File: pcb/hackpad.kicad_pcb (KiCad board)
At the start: 2 copper layers, 90 x 70 mm, 16 parts, among them J1 XIAO_L, J2 XIAO_R, J3 OLED, SW1 MX, SW2 MX, SW3 MX, SW4 MX

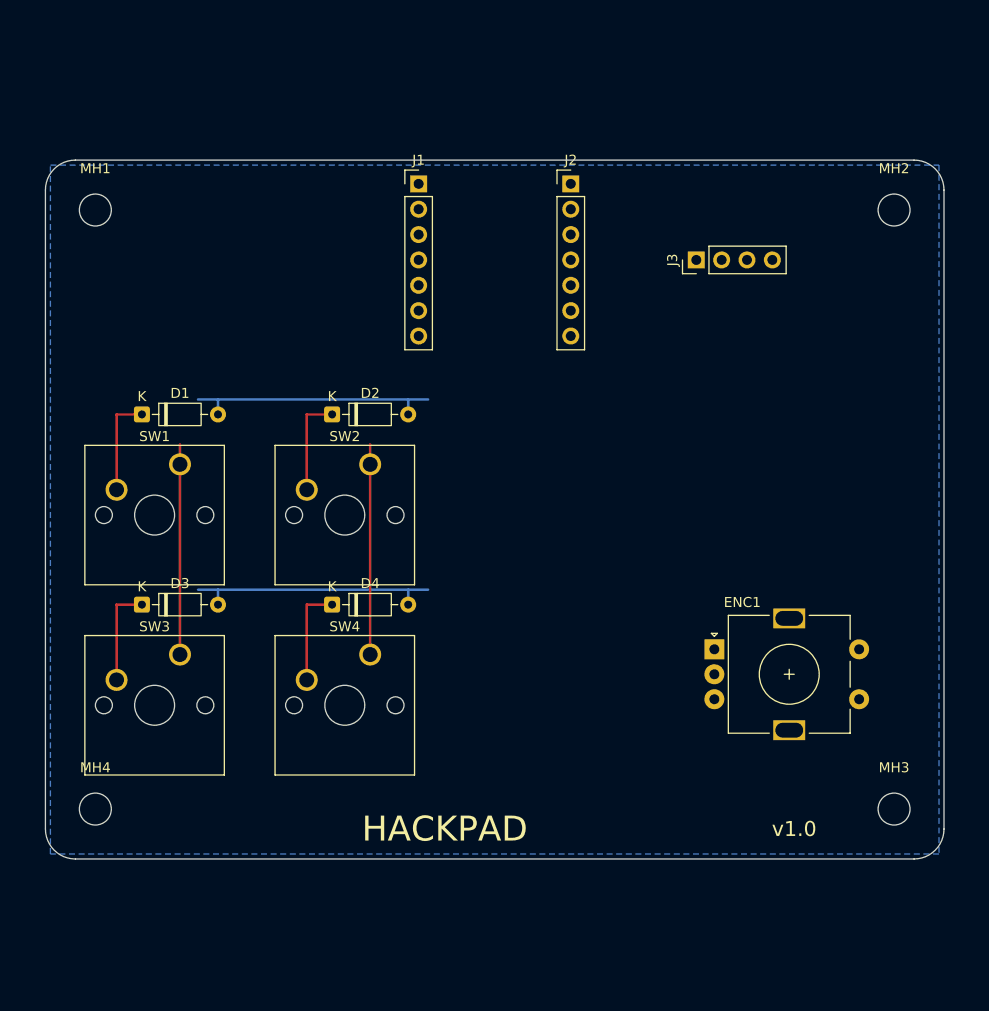
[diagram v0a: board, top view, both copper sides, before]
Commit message: v2: max-loaded build — 12 keys (4x3 matrix) + EC11 encoder + OLED
Surveyed 389 hackpads in hackclub/hackpad. Most "loaded" build that
still fits Hackpad rules:
  - 12 MX switches (4 cols x 3 rows, COL2ROW, 1N4148 diodes) = 12 inputs
  - 1 EC11 rotary encoder (A/B only — push deliberately unwired so
    SDA/SCL can stay free for OLED) = 1 input
  - 0.91" SSD1306 128x32 OLED on I2C1
  - 13 total inputs (under 16-input cap)
  - 95 x 95 mm board (under 100x100 cap)
  - All 11 usable XIAO RP2040 GPIO consumed (none spare)

PCB:
  - Matrix fully routed in copper (4 COL trunks F.Cu, 3 ROW trunks B.Cu
    with cathode tabs, 12 switch->anode bridges, GND pour, edge cuts)
  - 11 short XIAO->peripheral pulls left as ratlines for ~5 min
    interactive routing (each with exact start/end coords in
    pcb/HOW_TO_FINISH.md)
  - DRC passes at error level (0 violations, 0 unconnected)
  - New silkscreen: HACKPAD v2.0 front, github URL on back

Hardware as individual STL/STEP parts:
  - production/Top.{stl,step}                 (3D-printable)
  - production/Bottom.{stl,step}              (3D-printable)
  - production/M3x16_Screw.{stl,step}         (used x4 in assembly)
  - production/HeatsetInsert_M3x5x4.{stl,step} (used x4 in assembly)
  - cad/assembled-model.{step,stl} now includes the 4 screws + 4 inserts

Firmware: KMK with 3 layers (default letters / media / numpad), encoder
re-mapped per layer. OLED shows active layer name.

Mockup re-rendered to show the 12-key grid with 4 visible screw heads,
encoder knob, OLED window, HACK CLUB decal — saved to assets/mockup.png
and ~/Desktop/hackpad_mockup.png.

Re-exported production/gerbers.zip from the new .kicad_pcb.
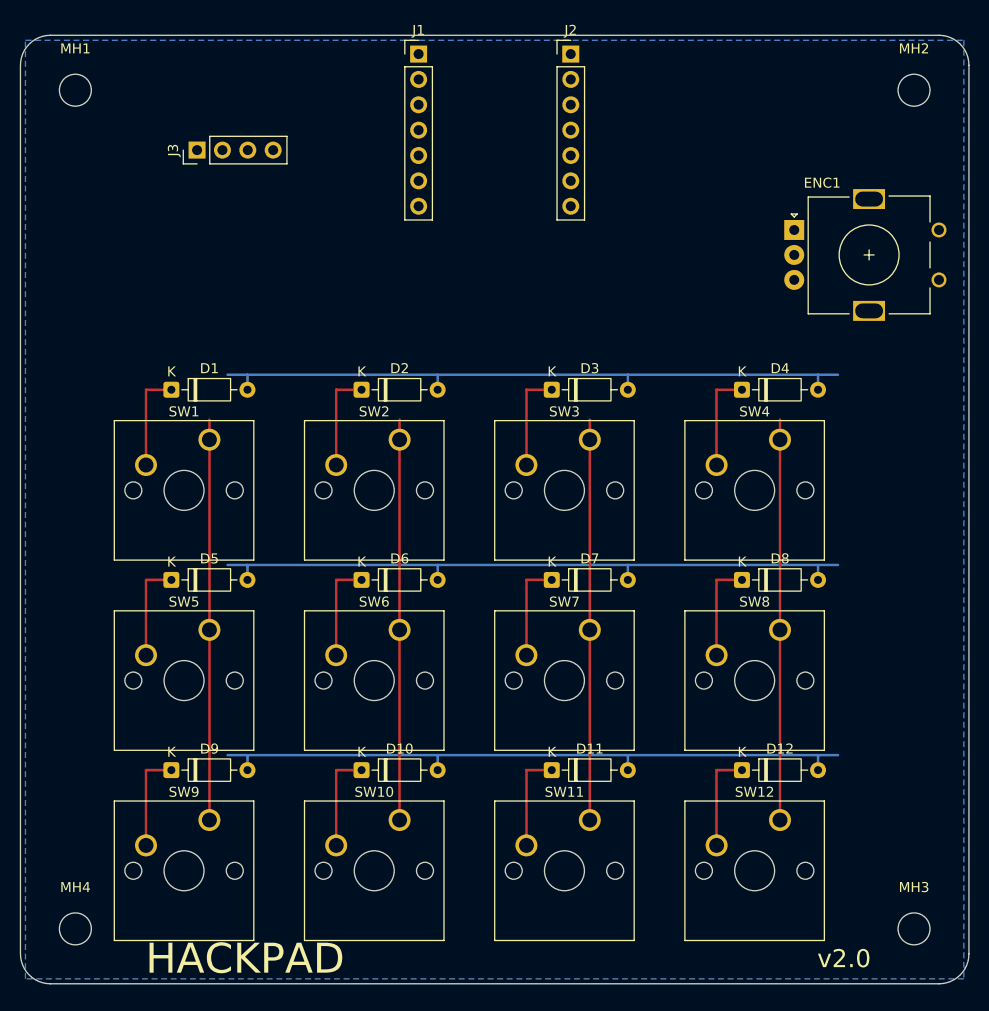
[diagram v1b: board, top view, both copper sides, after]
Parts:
- added D10: 1N4148, D_DO-35_SOD27_P7.62mm_Horizontal, F.Cu at (-13.3, 26.1)
- added D11: 1N4148, D_DO-35_SOD27_P7.62mm_Horizontal, F.Cu at (5.71, 26.1)
- added D12: 1N4148, D_DO-35_SOD27_P7.62mm_Horizontal, F.Cu at (24.8, 26.1)
- added D5: 1N4148, D_DO-35_SOD27_P7.62mm_Horizontal, F.Cu at (-32.4, 7.05)
- added D6: 1N4148, D_DO-35_SOD27_P7.62mm_Horizontal, F.Cu at (-13.3, 7.05)
- added D7: 1N4148, D_DO-35_SOD27_P7.62mm_Horizontal, F.Cu at (5.71, 7.05)
- added D8: 1N4148, D_DO-35_SOD27_P7.62mm_Horizontal, F.Cu at (24.8, 7.05)
- added D9: 1N4148, D_DO-35_SOD27_P7.62mm_Horizontal, F.Cu at (-32.4, 26.1)
- added SW10: MX, SW_Cherry_MX_1.00u_PCB, F.Cu at (-9.53, 31.1)
- added SW11: MX, SW_Cherry_MX_1.00u_PCB, F.Cu at (9.53, 31.1)
- added SW12: MX, SW_Cherry_MX_1.00u_PCB, F.Cu at (28.6, 31.1)
- added SW5: MX, SW_Cherry_MX_1.00u_PCB, F.Cu at (-28.6, 12.1)
- added SW6: MX, SW_Cherry_MX_1.00u_PCB, F.Cu at (-9.53, 12.1)
- added SW7: MX, SW_Cherry_MX_1.00u_PCB, F.Cu at (9.53, 12.1)
- added SW8: MX, SW_Cherry_MX_1.00u_PCB, F.Cu at (28.6, 12.1)
- added SW9: MX, SW_Cherry_MX_1.00u_PCB, F.Cu at (-28.6, 31.1)
- ENC1: footprint RotaryEncoder_Alps_EC11E-Switch_Vertical_H20mm -> RotaryEncoder_Alps_EC11E_Vertical_H20mm
- moved J3 51.2 mm to (-29.8, -36.0)
- moved D3 46.4 mm to (5.71, -12.0)
- moved D4 46.4 mm to (24.8, -12.0)
- moved SW3 46.4 mm to (9.53, -7.00)
- moved SW4 46.4 mm to (28.6, -7.00)
- moved ENC1 42.8 mm to (30.0, -28.0)
- moved J1 13.0 mm to (-7.62, -45.6)
- moved J2 13.0 mm to (7.62, -45.6)
- moved MH1 12.2 mm to (-42.0, -42.0)
- moved MH2 12.2 mm to (42.0, -42.0)
- moved MH3 12.2 mm to (42.0, 42.0)
- moved MH4 12.2 mm to (-42.0, 42.0)
- moved D1 3.85 mm to (-32.4, -12.0)
- moved D2 3.85 mm to (-13.3, -12.0)
- moved SW1 3.85 mm to (-28.6, -7.00)
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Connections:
- D3 pad 2: ROW1 -> ROW0
- D4 pad 2: ROW1 -> ROW0
- J1 pad 3: ENC_A -> COL2
- J1 pad 4: ENC_B -> COL3
- J2 pad 1: RGB_DIN -> ENC_B
- J2 pad 2: SPARE -> ENC_A
- J2 pad 3: ENC_PUSH -> ROW2
- SW3 pad 1: COL0 -> COL2
- SW4 pad 1: COL1 -> COL3
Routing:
- net ROW2: track 0.00 -> 67.2 mm
- net ROW1: track 26.1 -> 67.2 mm
- net ROW0: track 26.1 -> 67.2 mm
- net COL3: track 0.00 -> 40.1 mm
- net COL2: track 0.00 -> 40.1 mm
- net COL1: track 21.1 -> 40.1 mm
- net COL0: track 21.1 -> 40.1 mm
- net SW9_K: track 0.00 -> 10.1 mm
- net SW5_K: track 0.00 -> 10.1 mm
- net SW7_K: track 0.00 -> 10.1 mm
- net SW8_K: track 0.00 -> 10.1 mm
- net SW6_K: track 0.00 -> 10.1 mm
- net SW12_K: track 0.00 -> 10.1 mm
- net SW11_K: track 0.00 -> 10.1 mm
- net SW10_K: track 0.00 -> 10.1 mm
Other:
- board size 90 x 70 mm -> 95 x 95 mm
- board text added: "github.com/rishith-c/hackpad"
- board text added: "v2.0"
- board text removed: "v1.0"
